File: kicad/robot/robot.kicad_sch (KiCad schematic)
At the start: 58 parts, among them U1 DNP, U10 TPD1E05U06, U7 TPD1E05U06

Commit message: updated all footprint fields in schematic symbols with local robot ones
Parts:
- C1: footprint Capacitor_SMD:C_0603_1608Metric -> robot:C_0603_1608Metric
- H1, H2, H3, H4: footprint MountingHole:MountingHole_2.7mm_M2.5 -> robot:MountingHole_2.7mm_M2.5
- JP22: footprint custom_connectors:2.54mm_2pointJumper -> robot:2.54mm_2pointJumper
- JP7: footprint custom_connectors:2.54mm_2pointJumperClosed -> robot:2.54mm_2pointJumperClosed
- JP8, JP9: footprint custom_connectors:2.54mm_2pointJumperOpen -> robot:2.54mm_2pointJumperOpen
- R10, R11, R14, R15: footprint Resistor_SMD:R_0603_1608Metric -> robot:R_0603_1608Metric
- R6, R7: footprint Resistor_SMD:R_0402_1005Metric -> robot:R_0402_1005Metric
- S1, S3: footprint Button_Switch_SMD:Switch_Slide_JS202011SCQN -> robot:Switch_Slide_JS202011SCQN
- TP1, TP2, TP3, TP4, TP5, TP6: footprint TestPoint:KEYSTONE_5002 -> robot:KEYSTONE_5002
- U1: footprint Connector_JST:JST_SH_BM03B-SRSS-TB_1x03-1MP_P1.00mm_Vertical -> robot:JST_SH_BM03B-SRSS-TB_1x03-1MP_P1.00mm_Vertical
- U10, U7: footprint Package_X1SON:TPD1E05U06DPYR -> robot:TPD1E05U06DPYR

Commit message: Exported all schematic symbols to local robot and refer to them in all symbols
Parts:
- C1: symbol Device:C -> robot:C
- H1, H2, H3, H4: symbol Mechanical:MountingHole -> robot:MountingHole
- JP22: symbol Jumper:Jumper -> robot:Jumper
- JP7: symbol Jumper:Jumper_2_Bridged -> robot:Jumper_2_Bridged
- JP8: symbol Jumper:Jumper_2_Open -> robot:Jumper_2_Open_1
- JP9: symbol Jumper:Jumper_2_Open -> robot:Jumper_2_Open
- R10, R11, R14, R15, R6, R7: symbol Device:R -> robot:R
- S1, S3: symbol Switch:JS202011SCQN -> robot:JS202011SCQN
- TP1, TP2, TP3, TP4, TP5, TP6: symbol Connector:TestPoint -> robot:TestPoint
- U1: symbol custom_modules:WRM483265-10F5-12V-G -> robot:WRM483265-10F5-12V-G
- U10: symbol Diode:TPD1E05U06 -> robot:TPD1E05U06_1
- U7: symbol Diode:TPD1E05U06 -> robot:TPD1E05U06

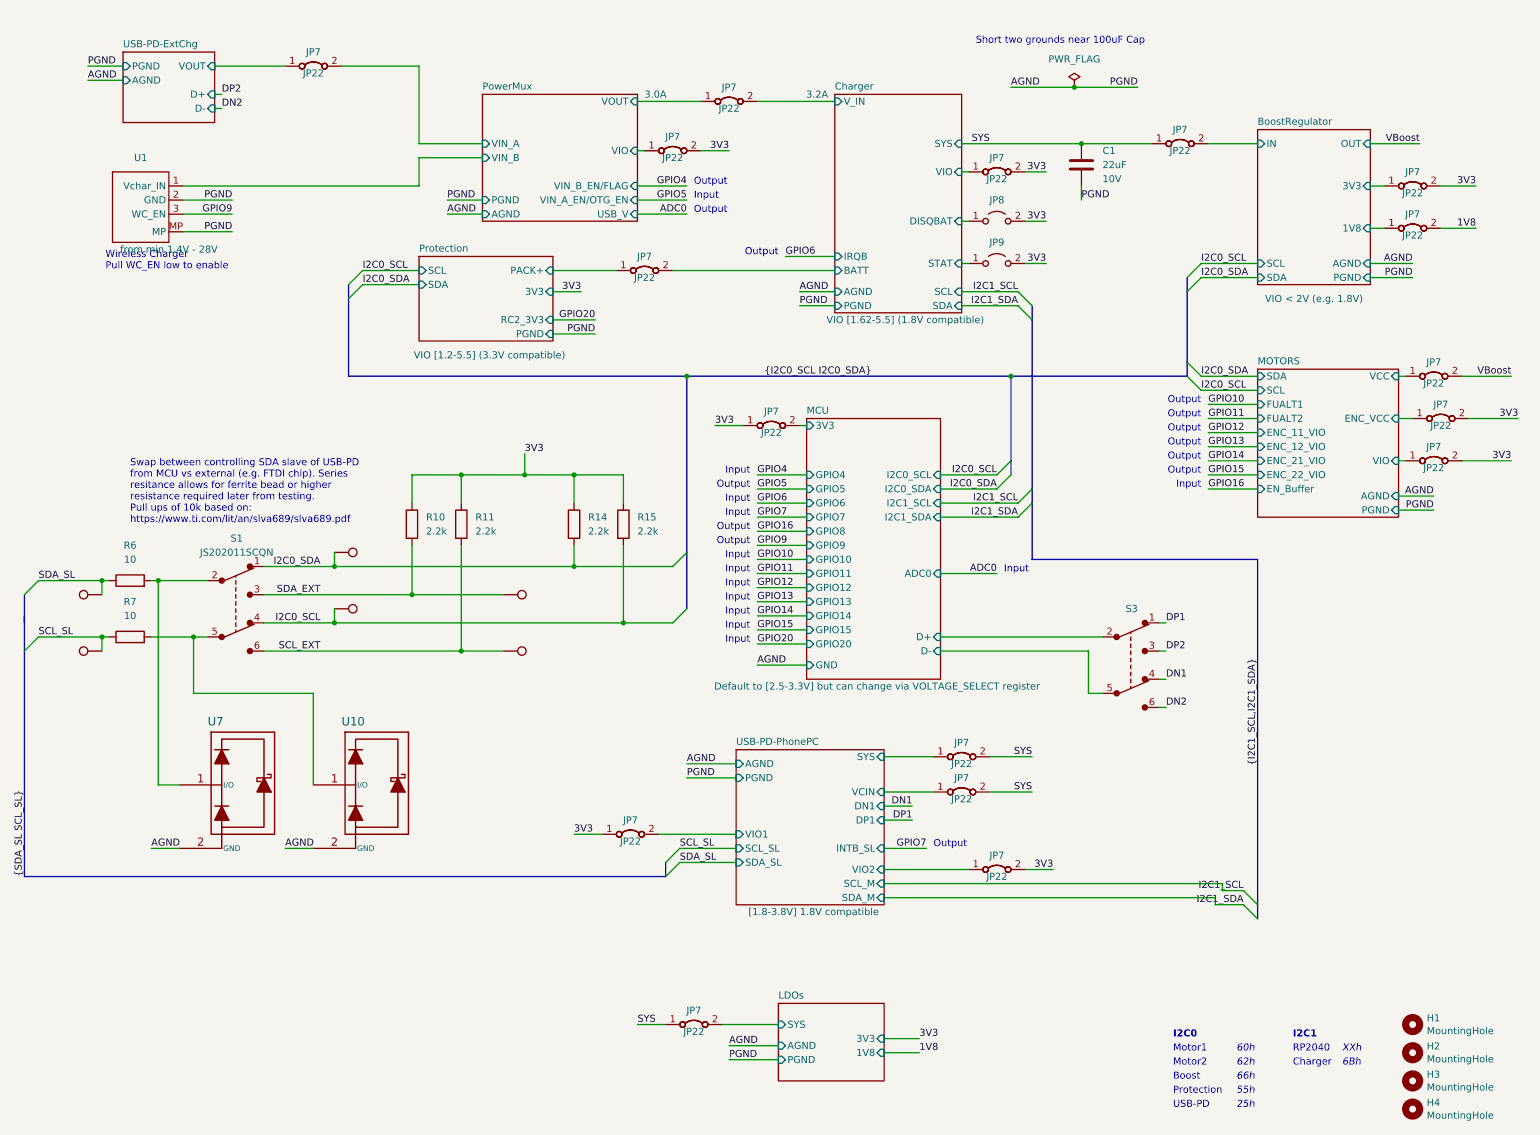
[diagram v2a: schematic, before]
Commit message: Replaced all jumpers with 0 ohm resistors
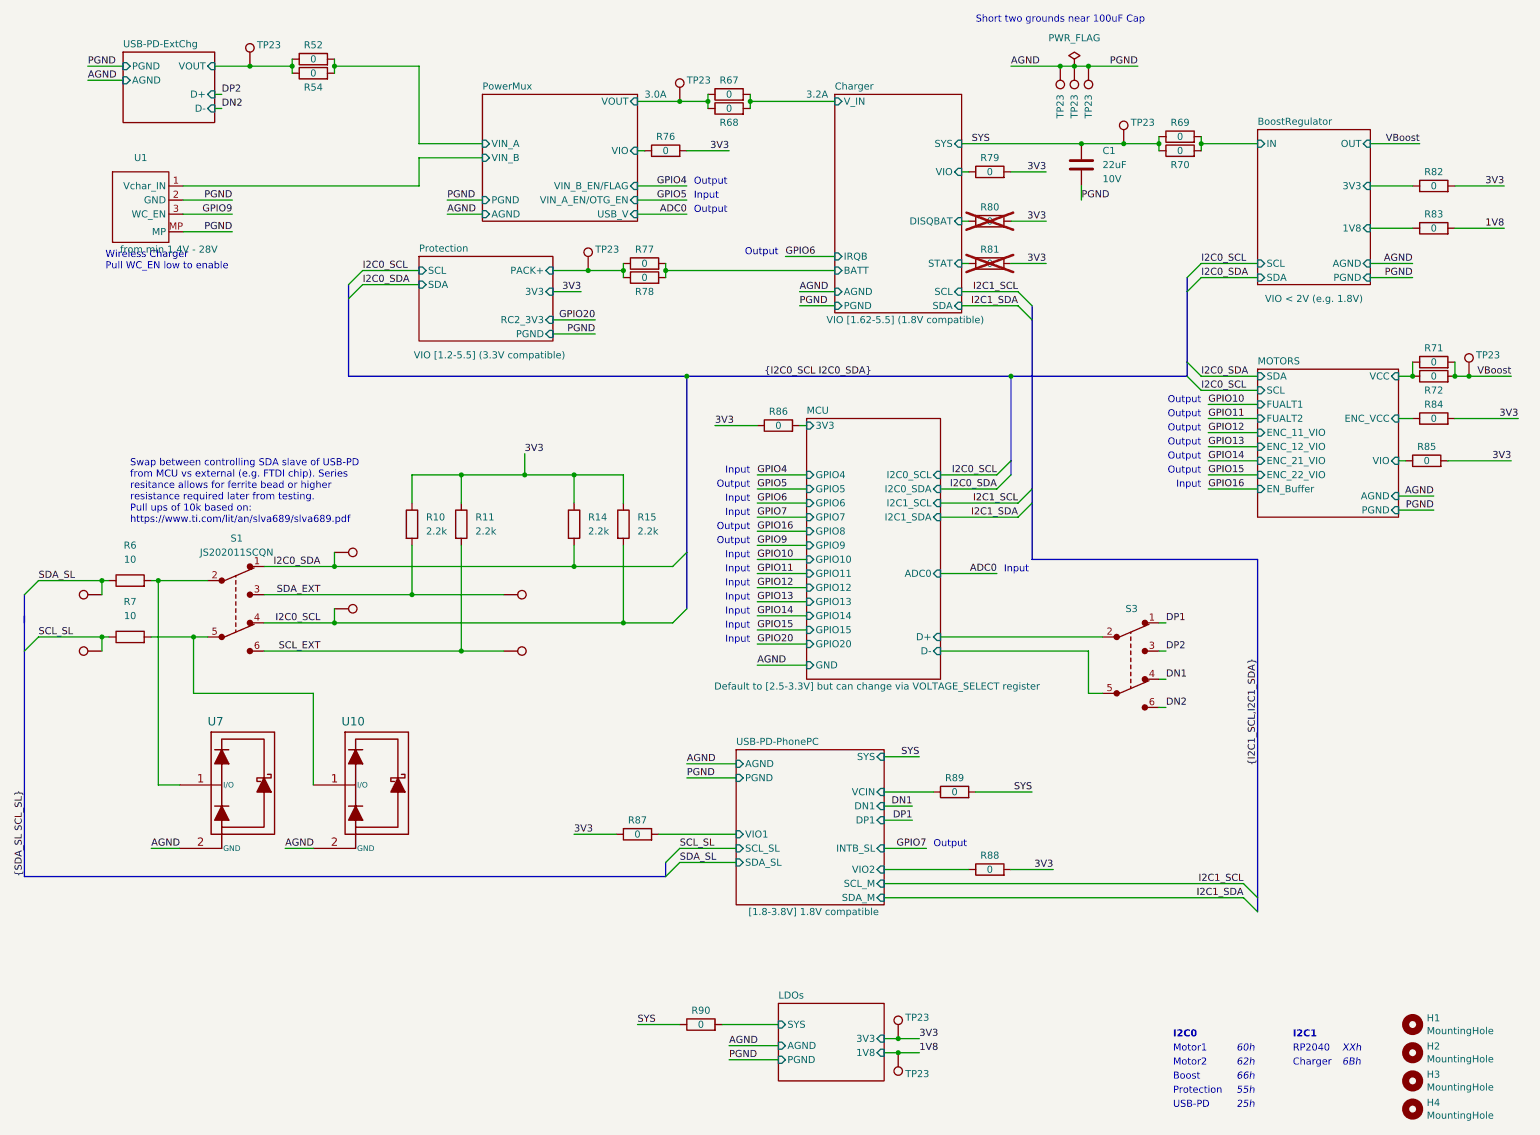
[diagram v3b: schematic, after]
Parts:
- removed JP22 (x17): Jumper, robot:2.54mm_2pointJumper, symbol robot:Jumper
- removed JP7 (x17): Jumper_Bridged, robot:2.54mm_2pointJumperClosed, symbol robot:Jumper_2_Bridged
- removed JP8: Jumper_Open, robot:2.54mm_2pointJumperOpen, symbol robot:Jumper_2_Open_1
- removed JP9: Jumper_Open, robot:2.54mm_2pointJumperOpen, symbol robot:Jumper_2_Open
- added R52, R54, R67, R68, R69, R70, R71, R72, R77, R78: 0, robot:R_0805_2012Metric, symbol Device:R
- added R76, R79, R80, R81, R82, R83, R84, R85, R86, R87, R88, R89, R90: 0, robot:R_0603_1608Metric, symbol Device:R
- added TP23 (x10): TestPoint, robot:KEYSTONE_5002, symbol robot:TestPoint
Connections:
- net 1V8: now also R83.2, TP23.1
- net 3V3: now also R76.2, R79.2, R80.2, R81.2, R82.2, R84.2, R85.2, R86.1, R87.1, R88.2, TP23.1
- net AGND: now also TP23.1, TP23.1, TP23.1
- net BoostRegulator/1V8: now also R83.1
- net BoostRegulator/3V3: now also R82.1
- net BoostRegulator/IN: now also R69.2, R70.2
- net Charger/BATT: now also R77.2, R78.2
- net Charger/DISQBAT: now also R80.1
- net Charger/STAT: now also R81.1
- net Charger/VIO: now also R79.1
- net Charger/V_IN: now also R67.2, R68.2
- net LDOs/SYS: now also R90.2
- net MCU/3V3: now also R86.2
- net MOTORS/ENC_VCC: now also R84.1
- net MOTORS/VCC: now also R71.1, R72.1
- net MOTORS/VIO: now also R85.1
- net PowerMux/VIN_A: now also R52.2, R54.2
- net PowerMux/VIO: now also R76.1
- net PowerMux/VOUT: now also R67.1, R68.1, TP23.1
- net Protection/PACK+: now also R77.1, R78.1, TP23.1
- net SYS: now also R69.1, R70.1, R89.2, R90.1, TP23.1
- net USB-PD-ExtChg/VOUT: now also R52.1, R54.1, TP23.1
- net USB-PD-PhonePC/VCIN: now also R89.1
- net USB-PD-PhonePC/VIO1: now also R87.2
- net USB-PD-PhonePC/VIO2: now also R88.1
- net VBoost: now also R71.2, R72.2, TP23.1

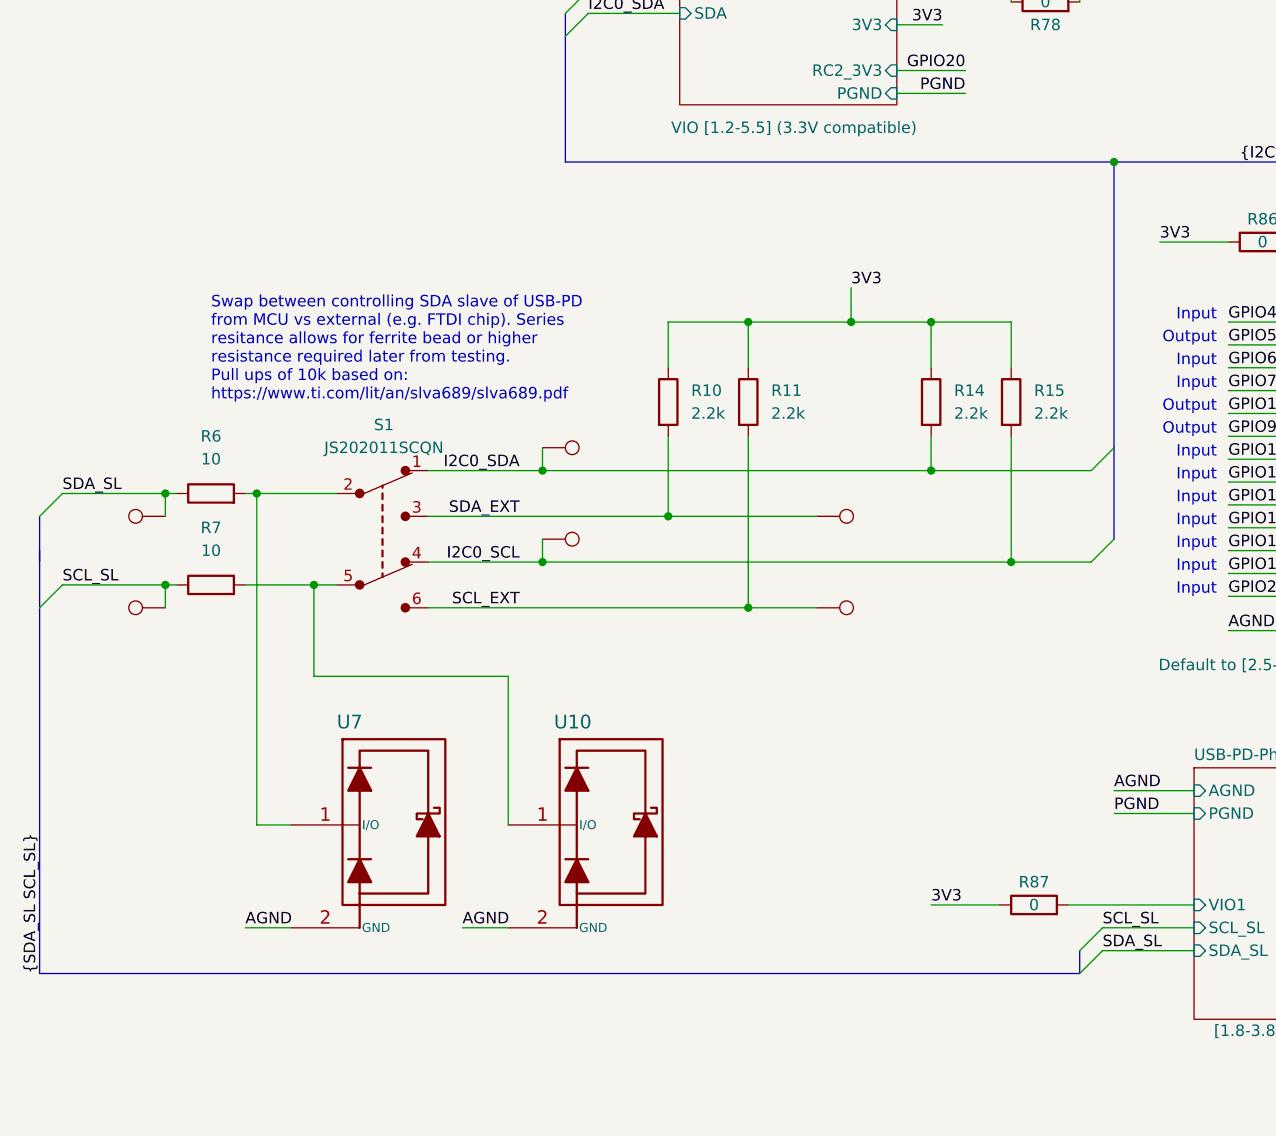
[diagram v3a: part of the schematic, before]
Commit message: removed i2c switch for external master. Not needed due to not using custom scripts on the Max77958 in favor of mcu control via firmware
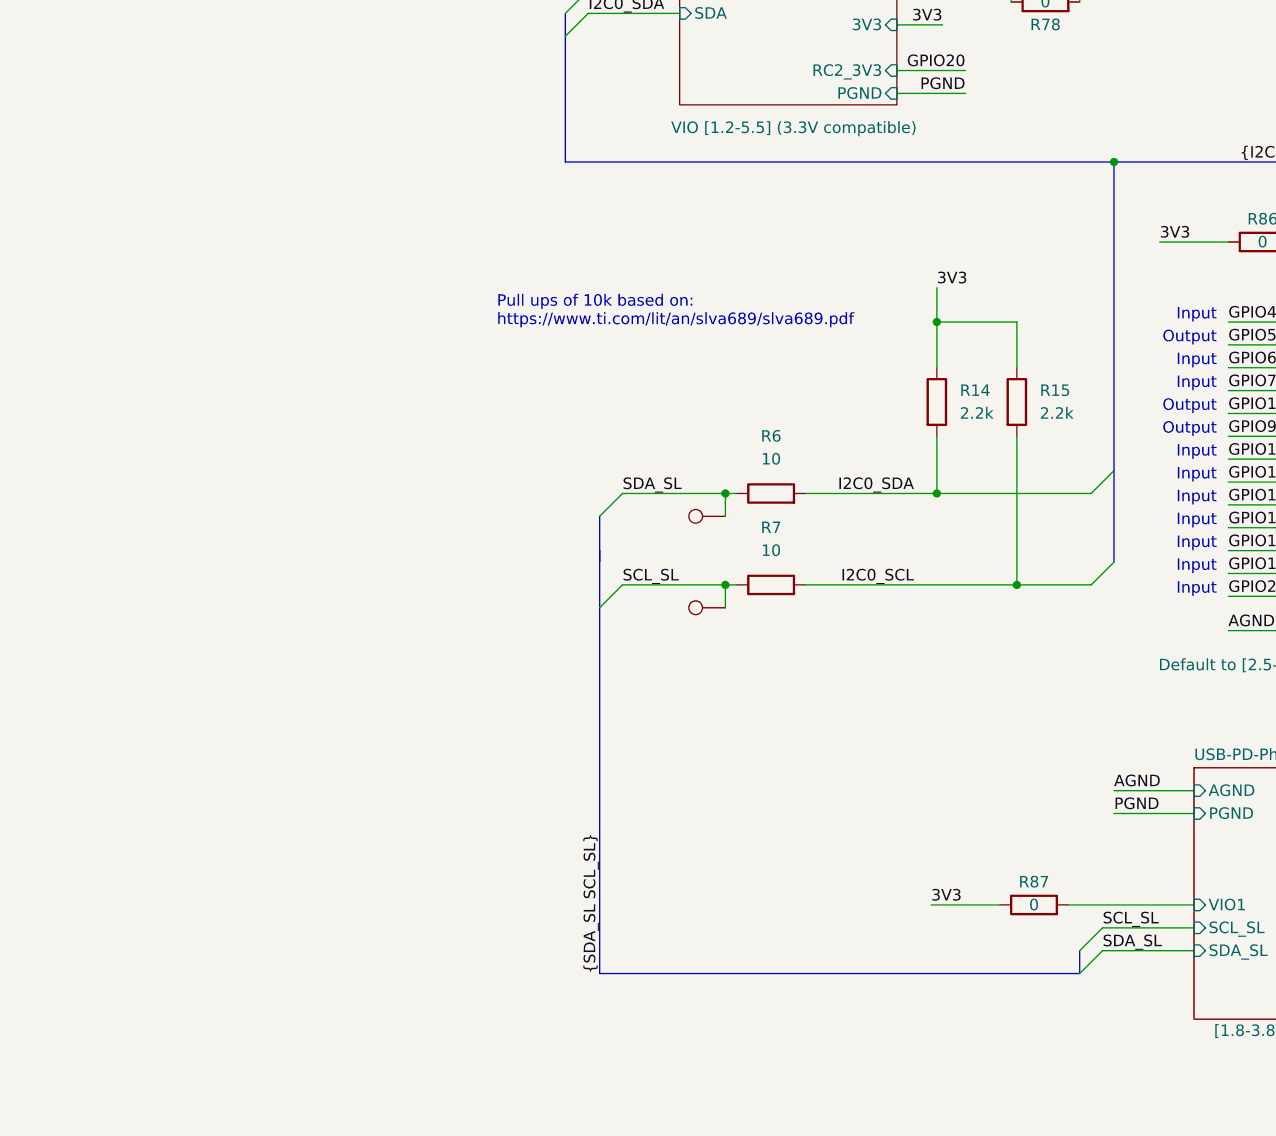
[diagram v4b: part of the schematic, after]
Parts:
- removed R10, R11: 2.2k, robot:R_0603_1608Metric, symbol robot:R
- removed S1: JS202011SCQN, robot:Switch_Slide_JS202011SCQN, symbol robot:JS202011SCQN
- removed TP3, TP4, TP5, TP6: TestPoint, robot:KEYSTONE_5002, symbol robot:TestPoint
- removed U10: TPD1E05U06, robot:TPD1E05U06DPYR, symbol robot:TPD1E05U06_1
- removed U7: TPD1E05U06, robot:TPD1E05U06DPYR, symbol robot:TPD1E05U06
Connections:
- net I2C0_SCL: now also R7.2
- net I2C0_SDA: now also R6.2
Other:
- note added: "Pull ups of 10k based on: https://www.ti.com/lit/an/slva689/slva689.pdf"
- note removed: "Swap between controlling SDA slave of USB-PD from MCU vs external (e.g. FTDI chip). Series resitance allows for ferrite bead or higher resistance required later from testing. Pull ups of 10k based on: https://www.ti.com/lit/an/slva689/slva689.pdf"
- moved on the sheet: R14, R15, R6, R7

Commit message: Adding JS202011JCQN to project in place of other switch
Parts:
- S3: value JS202011SCQN -> JS202011JCQN; footprint robot:Switch_Slide_JS202011SCQN -> robot:SW_JS202011JCQN; Digi-Key_PN 401-2002-1-ND -> (none); Part Number JS202011SCQN -> JS202011JCQN
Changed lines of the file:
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@@
       (effects (font (size 1.27 1.27)))
     )
-    (property "Value" "JS202011SCQN" (at 207.1624 118.11 0)
+    (property "Value" "JS202011JCQN" (at 207.1624 118.11 0)
       (effects (font (size 1.27 1.27)) hide)
     )
-    (property "Footprint" "robot:Switch_Slide_JS202011SCQN" (at 212.09 123.19 0)
+    (property "Footprint" "robot:SW_JS202011JCQN" (at 212.09 123.19 0)
       (effects (font (size 1.27 1.27)) (justify left) hide)
     )
@@
       (effects (font (size 1.524 1.524)) (justify left) hide)
     )
-    (property "Digi-Key_PN" "401-2002-1-ND" (at 212.09 118.11 0)
+    (property "Digi-Key_PN" "" (at 212.09 118.11 0)
       (effects (font (size 1.524 1.524)) (justify left) hide)
     )
@@
       (effects (font (size 1.524 1.524)) (justify left) hide)
     )
-    (property "Part Number" "JS202011SCQN" (at 207.01 128.27 0)
+    (property "Part Number" "JS202011JCQN" (at 207.01 128.27 0)
       (effects (font (size 1.27 1.27)) hide)
     )
